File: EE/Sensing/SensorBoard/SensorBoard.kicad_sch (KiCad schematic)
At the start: 10 parts

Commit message: WIP - TBs ordered, Sensor board pre layout sensor board
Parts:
- removed D?: D, symbol Device:D
- added H1, H2, H3, H4: MountingHole, MountingHole:MountingHole_2.5mm, symbol Mechanical:MountingHole
- U1: renamed from U?; value TCR2EE32 -> TCR2EE27
- gave numbers to parts that had none: 8
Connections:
- net 3v2 is gone; now on net 2v7: C4.1, U2.4 (VOUT)
- net 2v7: now reaches C3.1, U1.4 (VOUT)
- net 2v5_EN renamed 2v7_EN

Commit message: All on top layer
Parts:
- J1: footprint Connector_PinHeader_1.27mm:PinHeader_2x13_P1.27mm_Vertical -> Connector_PinHeader_1.27mm:PinHeader_2x13_P1.27mm_Vertical_SMD
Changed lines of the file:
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@@
     (property "Reference" "J1" (id 0) (at 261.112 37.1942 0))
     (property "Value" "Conn_02x13_Odd_Even" (id 1) (at 261.112 39.7311 0))
-    (property "Footprint" "Connector_PinHeader_1.27mm:PinHeader_2x13_P1.27mm_Vertical" (id 2) (at 259.842 57.404 0)
+    (property "Footprint" "Connector_PinHeader_1.27mm:PinHeader_2x13_P1.27mm_Vertical_SMD" (id 2) (at 259.842 57.404 0)
       (effects (font (size 1.27 1.27)) hide)
     )
@@
     )
     (path "/71ff8c52-c41a-4f55-80d4-34c20ea0aeb2"
-      (reference "J1") (unit 1) (value "Conn_02x13_Odd_Even") (footprint "Connector_PinHeader_1.27mm:PinHeader_2x13_P1.27mm_Vertical")
+      (reference "J1") (unit 1) (value "Conn_02x13_Odd_Even") (footprint "Connector_PinHeader_1.27mm:PinHeader_2x13_P1.27mm_Vertical_SMD")
     )
     (path "/47f064f1-bd7b-45b9-856e-c0759779ab1e/2790d670-1c79-4cf6-82ba-7ed5af0558fe"

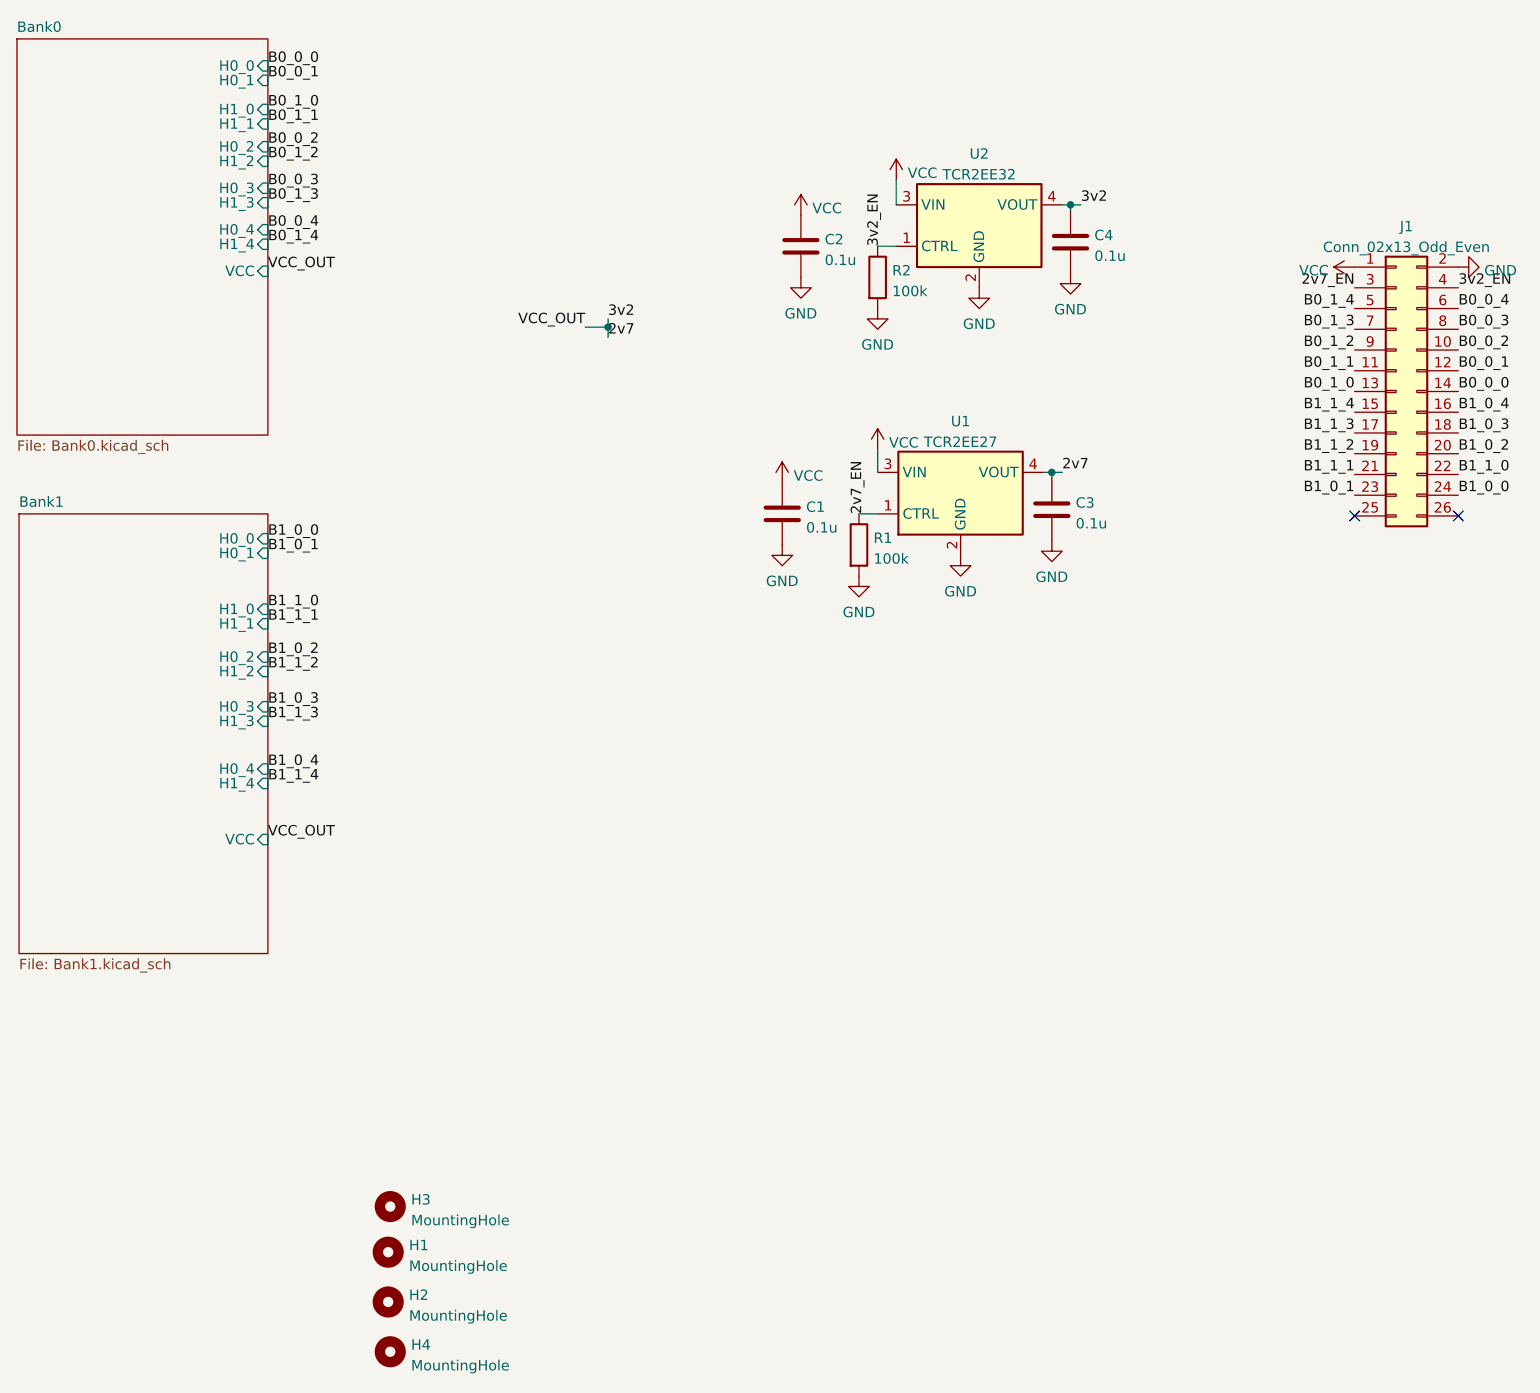
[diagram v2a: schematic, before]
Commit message: Sensors attached to mainboard
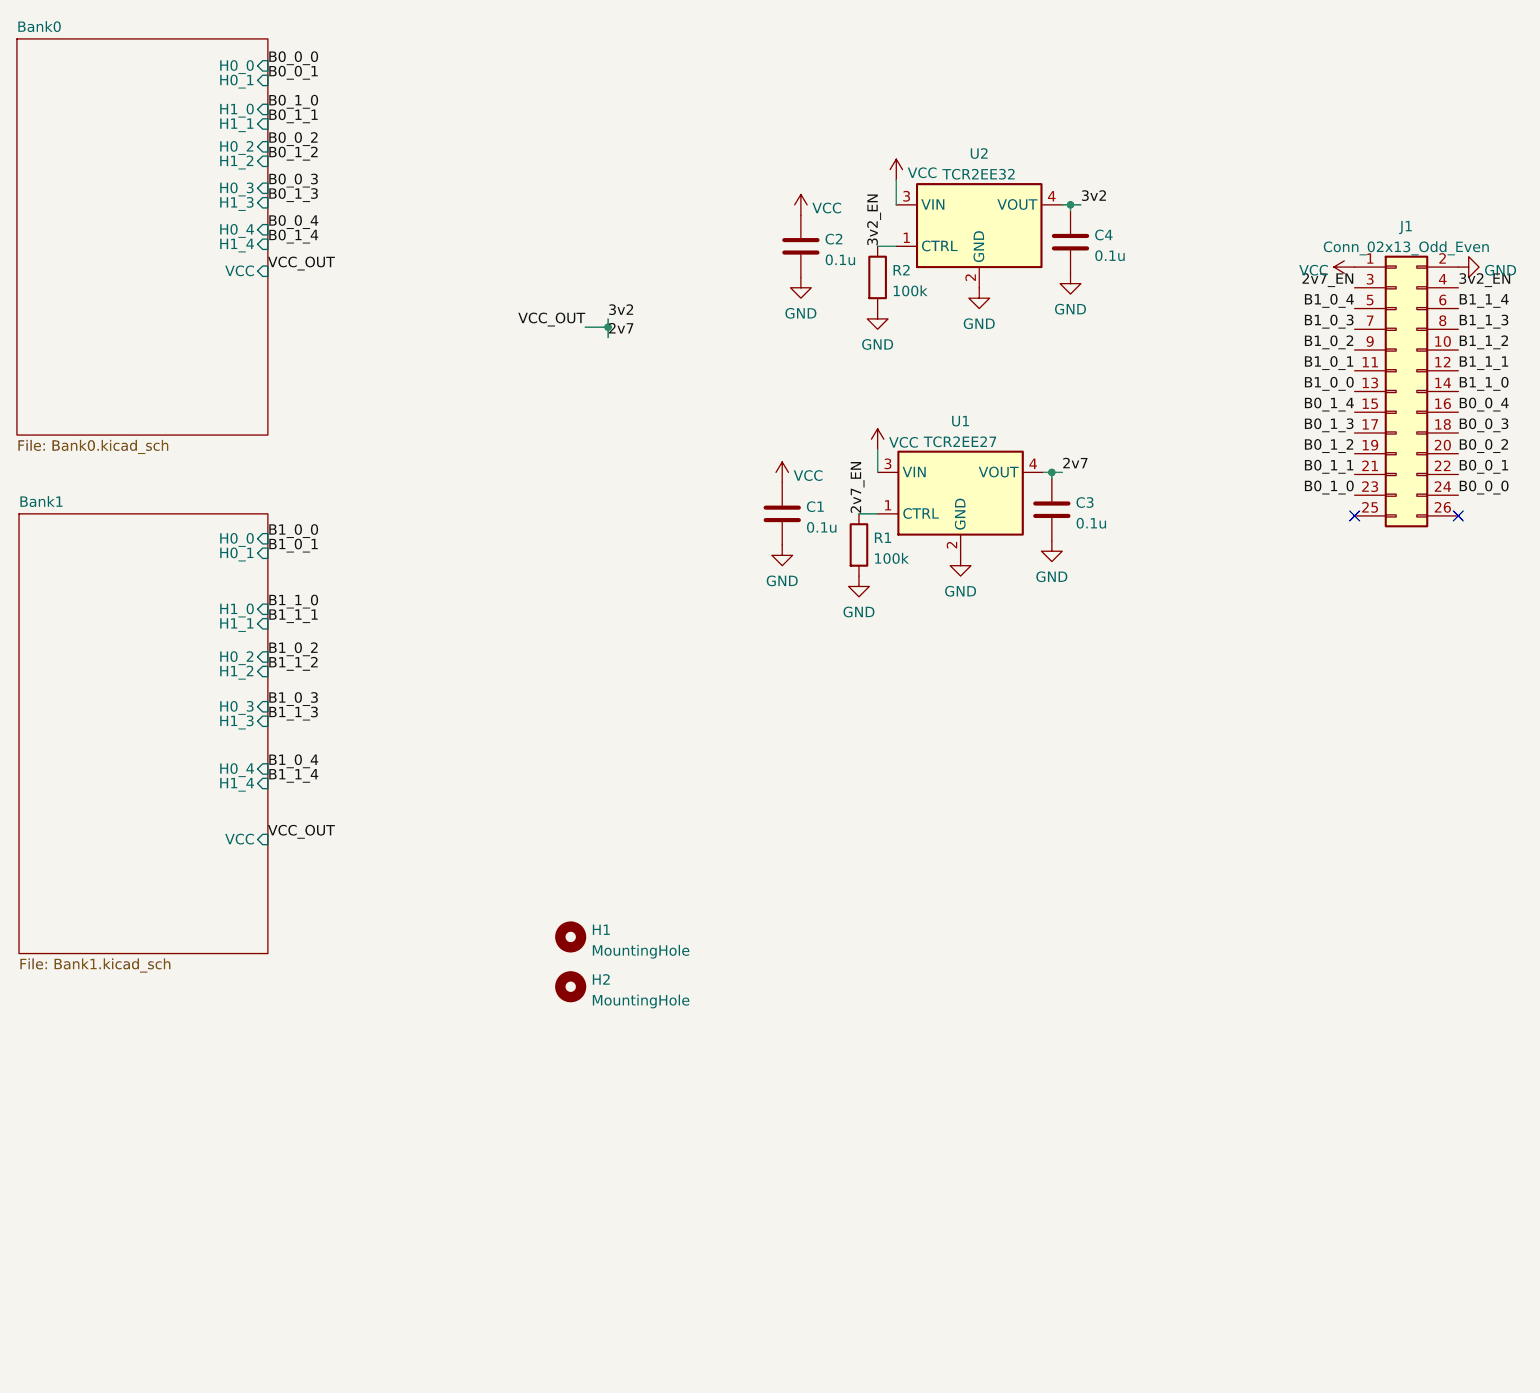
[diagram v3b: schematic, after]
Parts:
- removed H3, H4: MountingHole, MountingHole:MountingHole_2.5mm, symbol Mechanical:MountingHole
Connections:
- net B0_0_0: now also J1.24 (Pin_24); no longer J1.14 (Pin_14)
- net B0_0_1: now also J1.22 (Pin_22); no longer J1.12 (Pin_12)
- net B0_0_2: now also J1.20 (Pin_20); no longer J1.10 (Pin_10)
- net B0_0_3: now also J1.18 (Pin_18); no longer J1.8 (Pin_8)
- net B0_0_4: now also J1.16 (Pin_16); no longer J1.6 (Pin_6)
- net B0_1_0: now also J1.23 (Pin_23); no longer J1.13 (Pin_13)
- net B0_1_1: now also J1.21 (Pin_21); no longer J1.11 (Pin_11)
- net B0_1_2: now also J1.19 (Pin_19); no longer J1.9 (Pin_9)
- net B0_1_3: now also J1.17 (Pin_17); no longer J1.7 (Pin_7)
- net B0_1_4: now also J1.15 (Pin_15); no longer J1.5 (Pin_5)
- net B1_0_0: now also J1.13 (Pin_13); no longer J1.24 (Pin_24)
- net B1_0_1: now also J1.11 (Pin_11); no longer J1.23 (Pin_23)
- net B1_0_2: now also J1.9 (Pin_9); no longer J1.20 (Pin_20)
- net B1_0_3: now also J1.7 (Pin_7); no longer J1.18 (Pin_18)
- net B1_0_4: now also J1.5 (Pin_5); no longer J1.16 (Pin_16)
- net B1_1_0: now also J1.14 (Pin_14); no longer J1.22 (Pin_22)
- net B1_1_1: now also J1.12 (Pin_12); no longer J1.21 (Pin_21)
- net B1_1_2: now also J1.10 (Pin_10); no longer J1.19 (Pin_19)
- net B1_1_3: now also J1.8 (Pin_8); no longer J1.17 (Pin_17)
- net B1_1_4: now also J1.6 (Pin_6); no longer J1.15 (Pin_15)
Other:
- moved on the sheet: H1, H2

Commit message: WIP - Moving Sensor to IO Expander
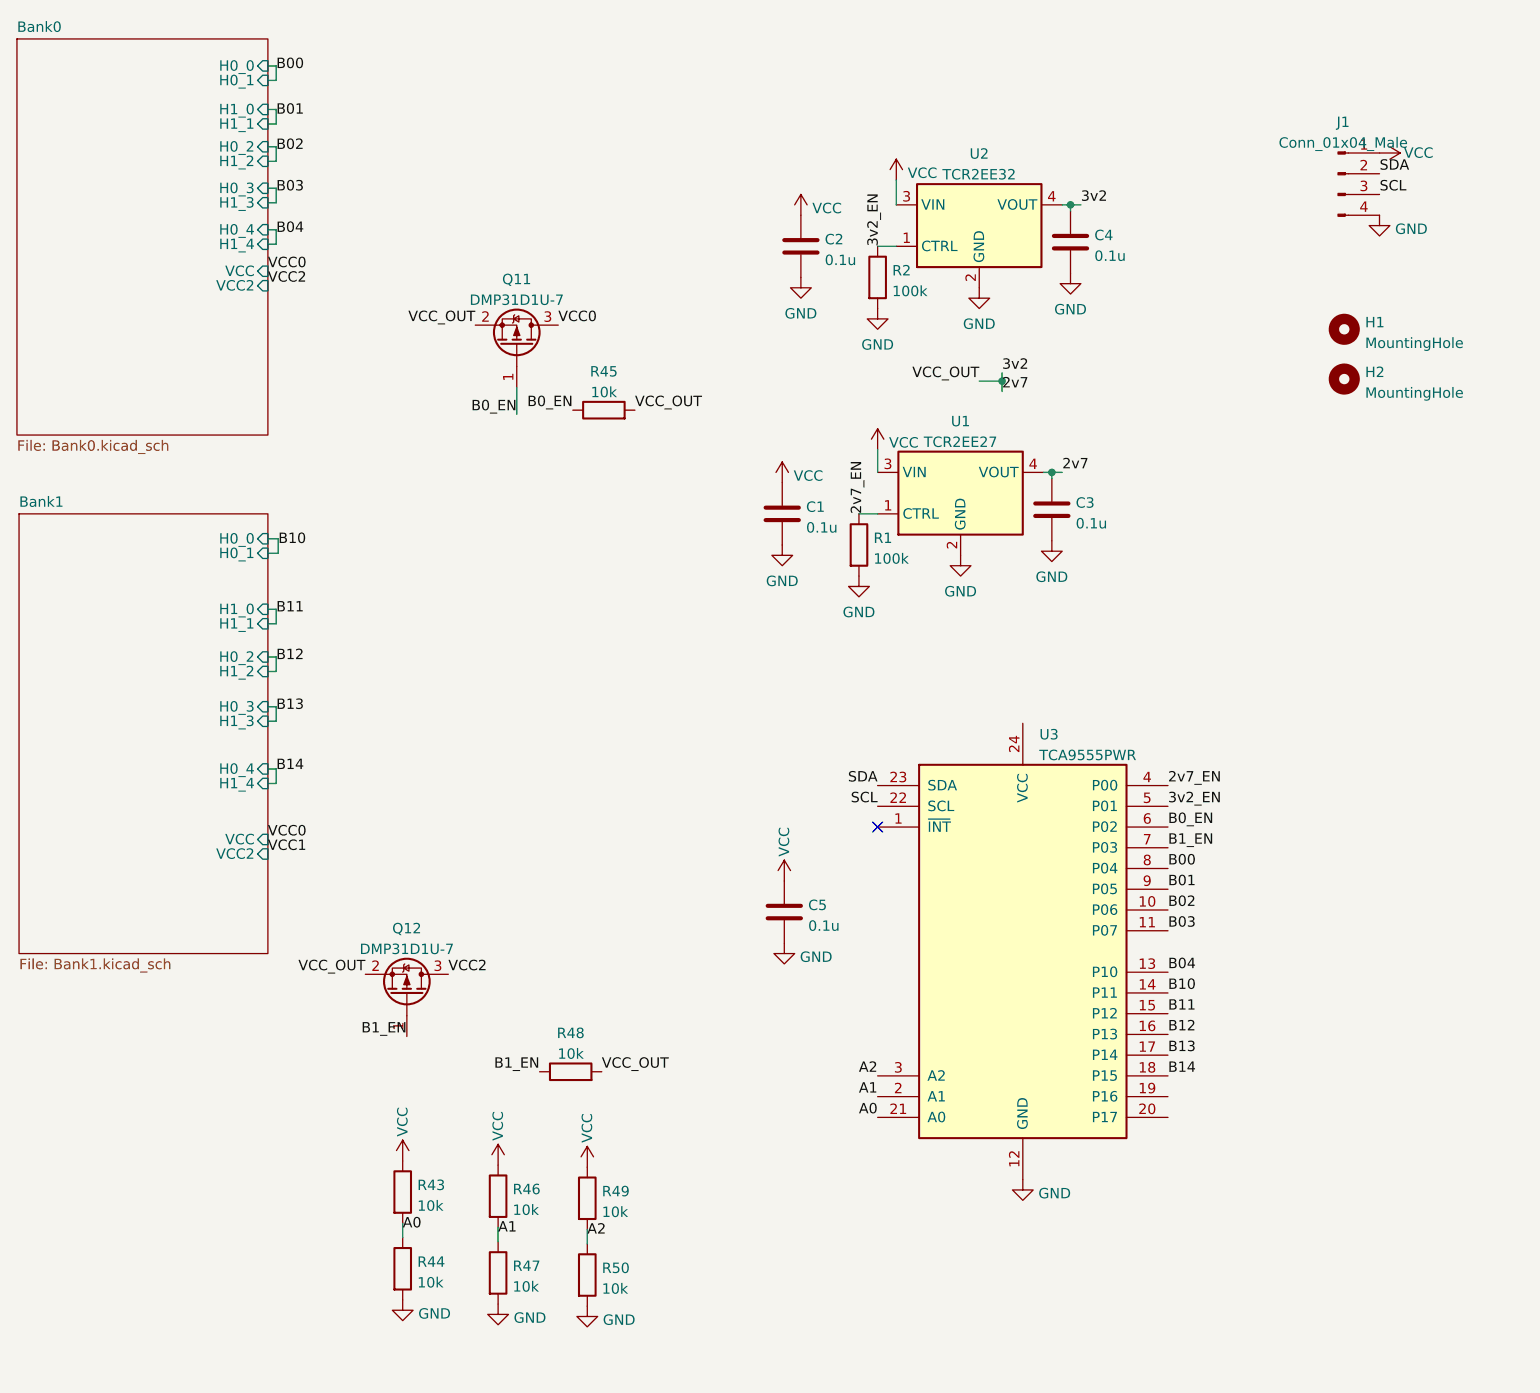
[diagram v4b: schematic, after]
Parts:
- removed J1: Conn_02x13_Odd_Even, Connector_PinHeader_1.27mm:PinHeader_2x13_P1.27mm_Vertical_SMD, symbol Connector_Generic:Conn_02x13_Odd_Even
- added C5: 0.1u, Capacitor_SMD:C_0402_1005Metric, symbol Device:C
- added J1: Conn_01x04_Male, Connector_PinSocket_2.54mm:PinSocket_1x04_P2.54mm_Vertical, symbol Connector:Conn_01x04_Male
- added Q11, Q12: DMP31D1U-7, Package_TO_SOT_SMD:SC-59, symbol Device:Q_PMOS_GSD
- added R43, R44, R45, R46, R47, R48, R49, R50: 10k, Resistor_SMD:R_0402_1005Metric, symbol Device:R
- added U3: TCA9555PWR, Package_SO:TSSOP-24_4.4x7.8mm_P0.65mm, symbol Interface_Expansion:TCA9555PWR
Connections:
- net 2v7: now also Q11.2 (S), Q12.2 (S), R45.2, R48.2
- net 2v7_EN: now also U3.4 (P00)
- net 3v2_EN: now also U3.5 (P01)
- net GND: now also C5.2, J1.4 (Pin_4), R44.2, R47.2, R50.2, U3.12 (GND)
- net VCC: now also C5.1, J1.1 (Pin_1), R43.1, R46.1, R49.1
- new net A0: R43.2, R44.1, U3.21 (A0)
- new net A1: R46.2, R47.1, U3.2 (A1)
- new net A2: R49.2, R50.1, U3.3 (A2)
- new net B00: U3.8 (P04)
- new net B01: U3.9 (P05)
- new net B02: U3.10 (P06)
- new net B03: U3.11 (P07)
- new net B04: U3.13 (P10)
- new net B0_EN: Q11.1 (G), R45.1, U3.6 (P02)
- new net B10: U3.14 (P11)
- new net B11: U3.15 (P12)
- new net B12: U3.16 (P13)
- new net B13: U3.17 (P14)
- new net B14: U3.18 (P15)
- new net B1_EN: Q12.1 (G), R48.1, U3.7 (P03)
- new net SCL: J1.3 (Pin_3), U3.22 (SCL)
- new net SDA: J1.2 (Pin_2), U3.23 (SDA)
- new net VCC0: Q11.3 (D)
- new net VCC2: Q12.3 (D)
- no-connect marks 2 -> 1
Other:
- sheet Bank0 ports: added VCC2; removed none
- sheet Bank1 ports: added VCC2; removed none
- moved on the sheet: H1, H2

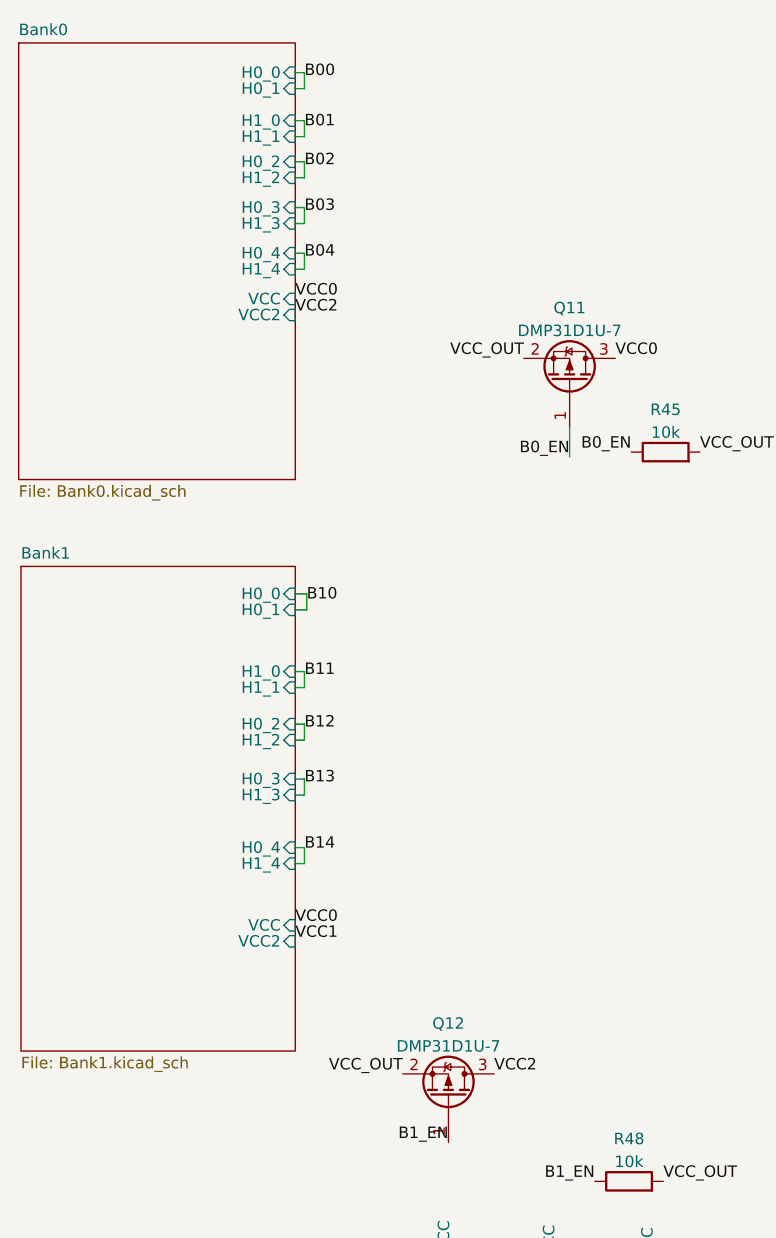
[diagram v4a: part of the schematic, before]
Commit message: Fix of Multiplexing
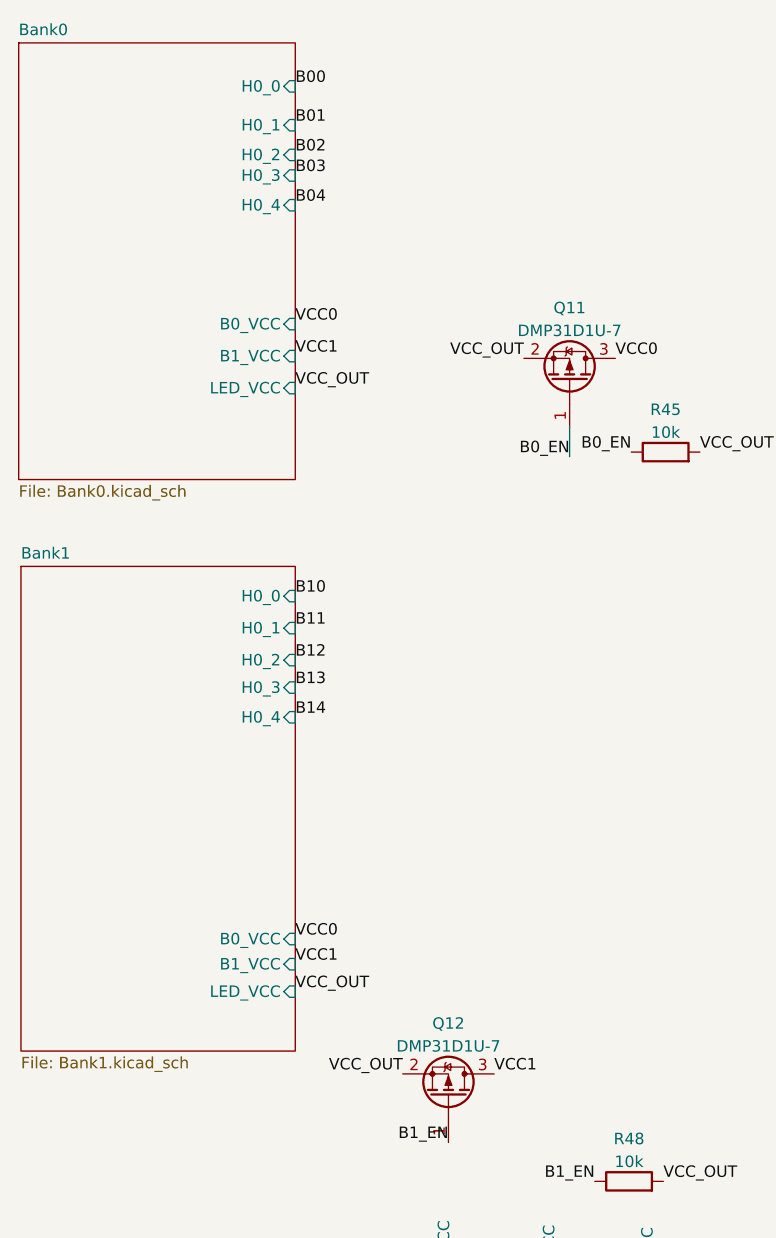
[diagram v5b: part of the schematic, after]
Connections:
- net VCC2 is gone; now on net VCC1: Q12.3 (D)
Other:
- sheet Bank0 ports: added B0_VCC, B1_VCC, LED_VCC; removed H1_0, H1_1, H1_2, H1_3, H1_4, VCC, VCC2
- sheet Bank1 ports: added B0_VCC, B1_VCC, LED_VCC; removed H1_0, H1_1, H1_2, H1_3, H1_4, VCC, VCC2
